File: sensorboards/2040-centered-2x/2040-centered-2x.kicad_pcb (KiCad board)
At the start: 2 copper layers, 20.5 x 48 mm, 5 parts, among them J1 Conn_01x06_Male, U1 CNY70, U2 CNY70

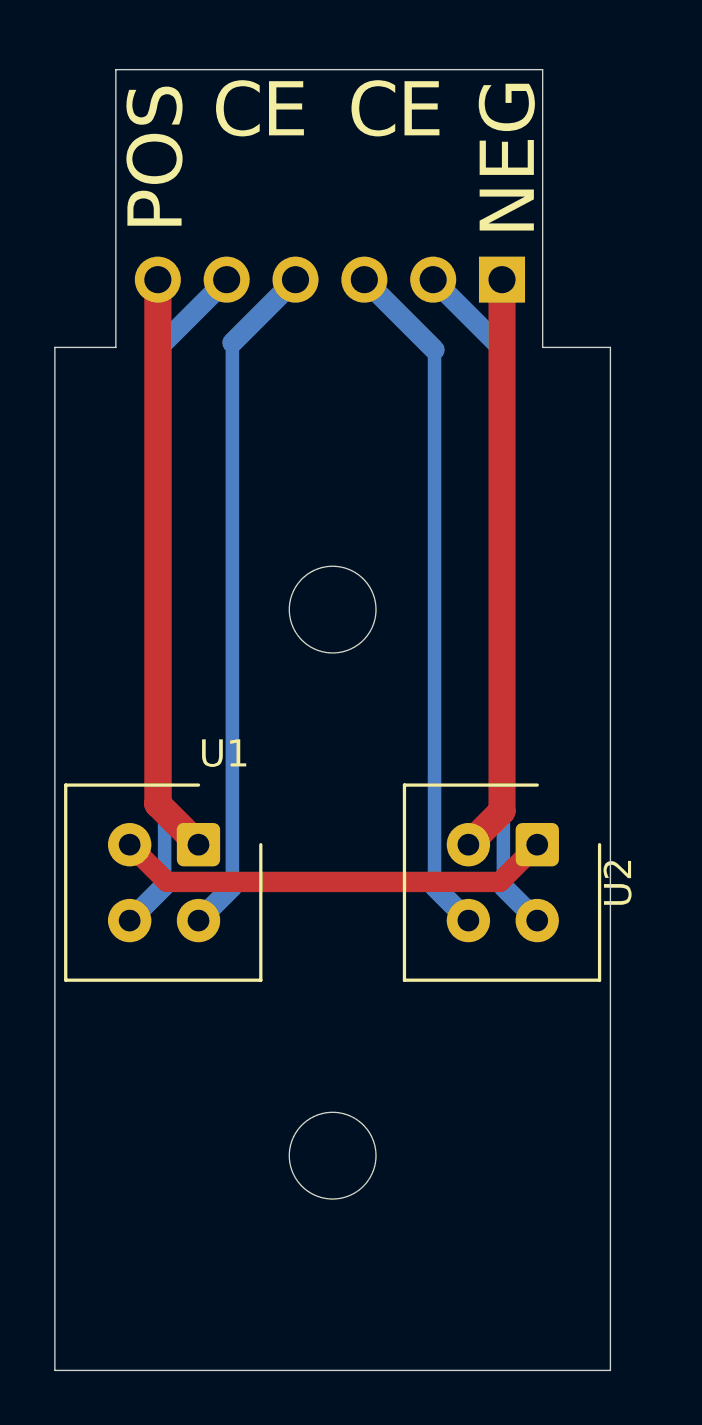
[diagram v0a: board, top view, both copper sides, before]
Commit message: Made issue #44 changes to sensorboards, introduced 3x versions
Also finished bringing them up to Kicad 6.0
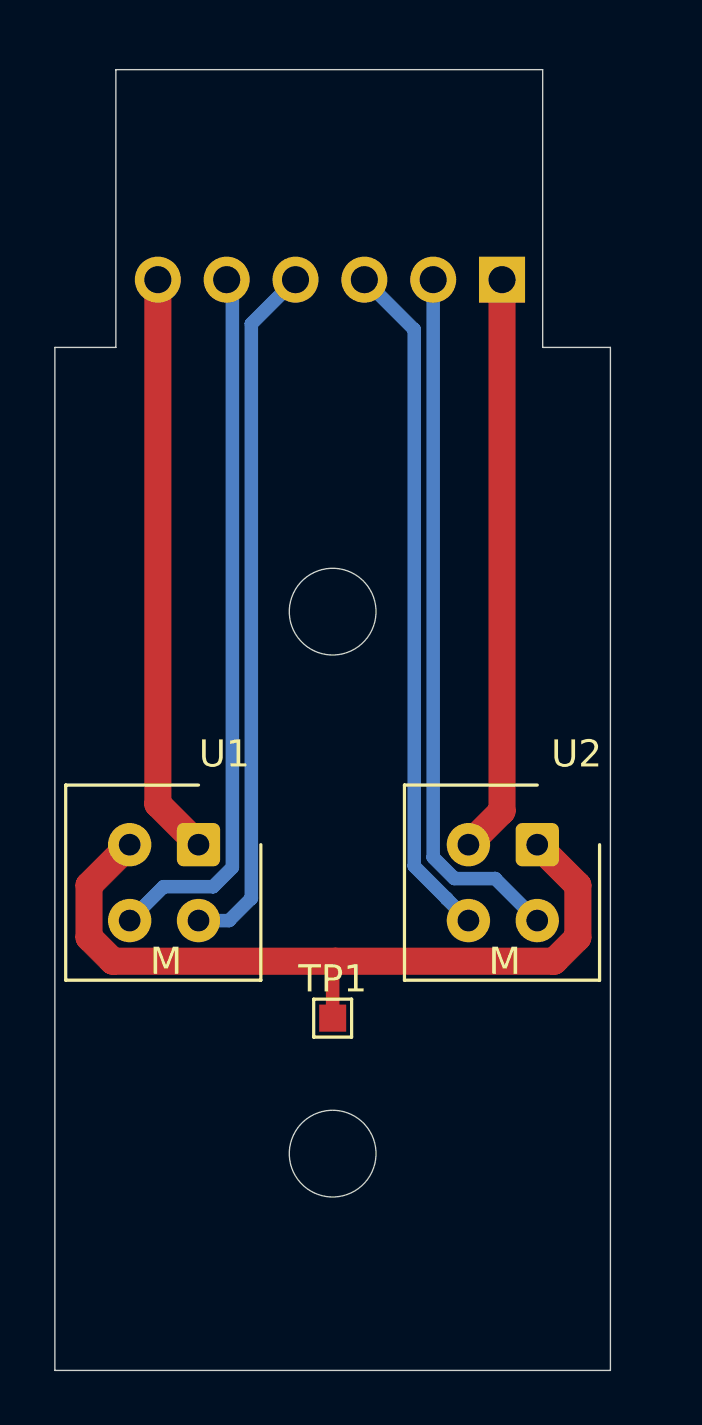
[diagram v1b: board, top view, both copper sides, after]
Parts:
- added TP1: TestPoint, TestPoint:TestPoint_Pad_1.0x1.0mm, F.Cu at (175.2, 125.0)
- moved H2 0.08 mm to (175.2, 110.0)
- moved H1 0.07 mm to (175.2, 130.0)
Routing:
- net Net-(U1-Pad2): track 16.2 -> 29.0 mm
- net Net-(J1-Pad5): track 25.1 -> 26.4 mm
- net Net-(J1-Pad2): track 25.2 -> 26.1 mm
- net Net-(J1-Pad4): track 25.1 -> 25.8 mm
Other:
- net class Default removed
